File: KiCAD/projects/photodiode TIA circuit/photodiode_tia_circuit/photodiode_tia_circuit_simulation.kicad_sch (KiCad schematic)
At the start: 8 parts, among them U2 ${SIM.PARAMS}, U3 ${SIM.PARAMS}

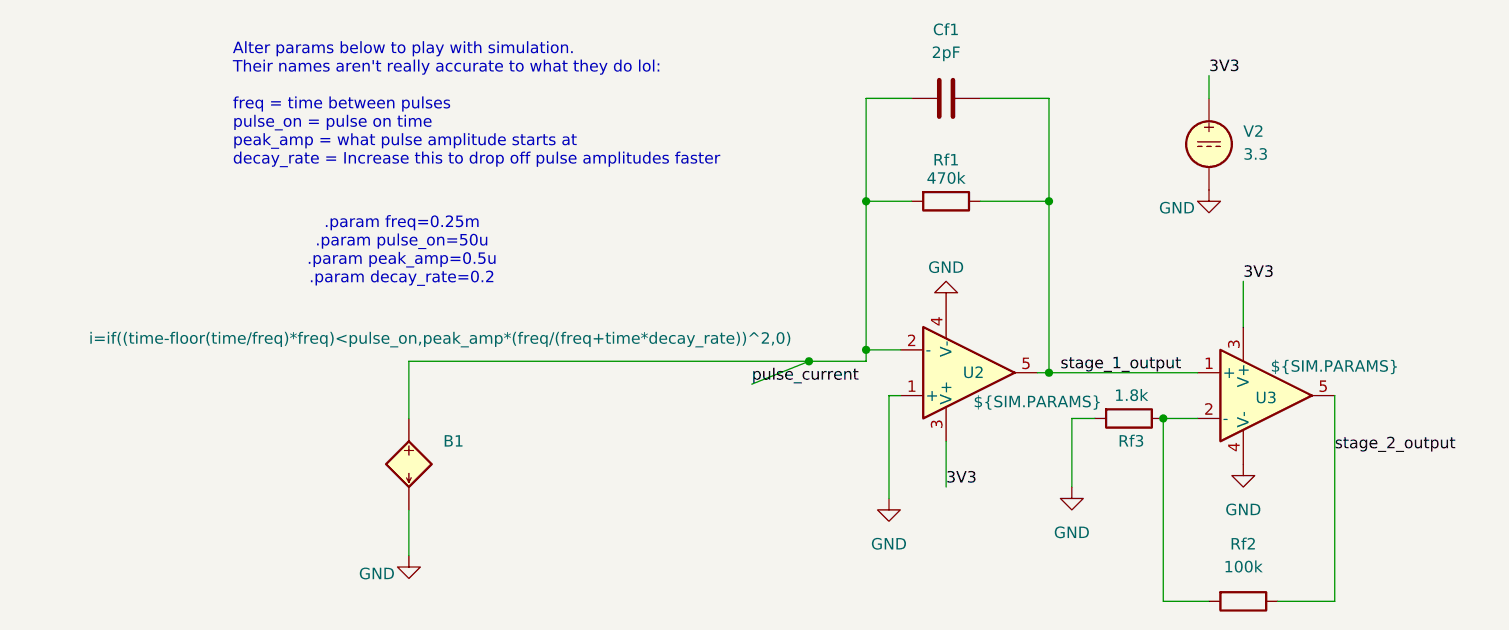
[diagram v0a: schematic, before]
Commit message: Update to make more sense and have flat-topped pulses
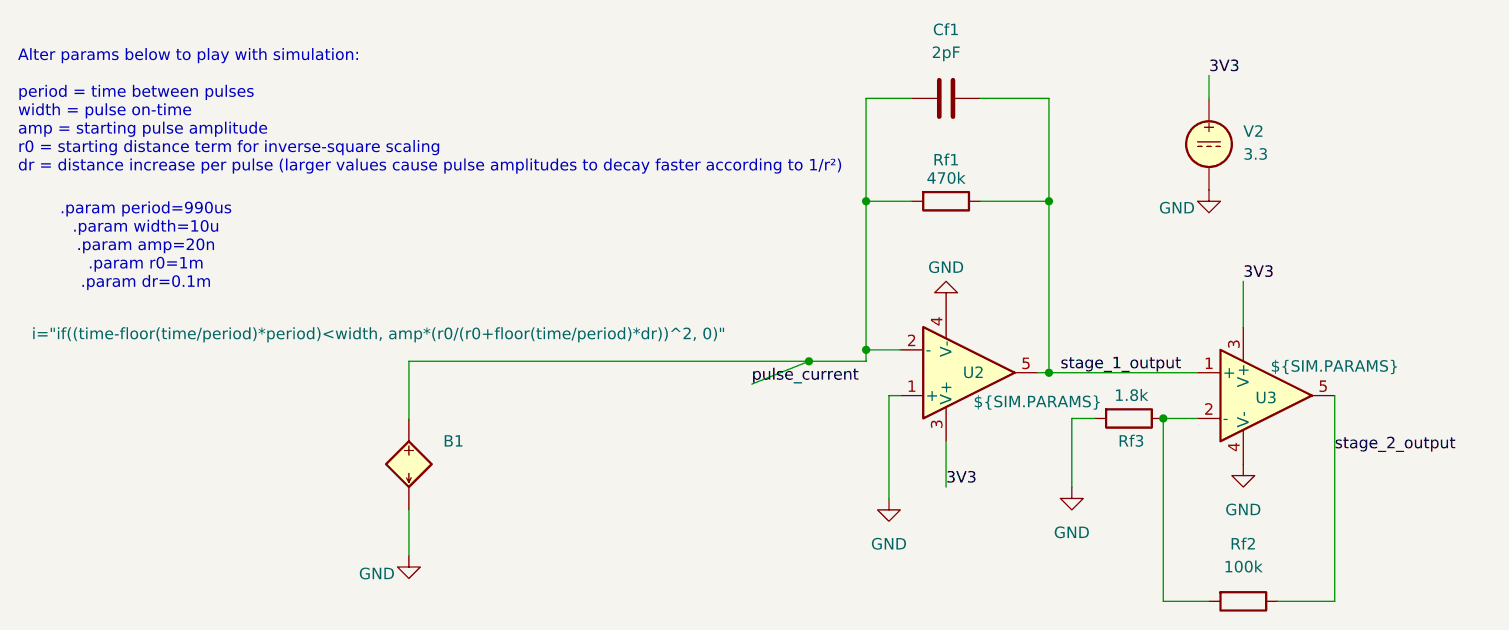
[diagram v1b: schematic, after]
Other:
- note added: ".param period=990us .param width=10u .param amp=20n .param r0=1m .param dr=0.1m"
- note added: "Alter params below to play with simulation: period = time between pulses width = pulse on-time amp = starting pulse amplitude r0 = starting distance term for inverse-square scaling dr = distance increase per pulse (larger values cause pulse amplitudes to decay faster according to 1/r²)"
- note removed: ".param freq=0.25m .param pulse_on=50u .param peak_amp=0.5u .param decay_rate=0.2"
- note removed: "Alter params below to play with simulation. Their names aren't really accurate to what they do lol: freq = time between pulses pulse_on = pulse on time peak_amp = what pulse amplitude starts at decay_rate = Increase this to drop off pulse amplitudes faster"
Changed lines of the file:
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@@
 	(generator_version "10.0")
 	(paper "A4")
-	(text ".param freq=0.25m\n.param pulse_on=50u\n.param peak_amp=0.5u\n.param decay_rate=0.2"
+	(text ".param period=990us \n.param width=10u\n.param amp=20n \n.param r0=1m \n.param dr=0.1m"
 		(exclude_from_sim no)
-		(at 62.738 103.378 0)
+		(at 34.29 102.87 0)
 		(effects
 			(font
@@
 		)
 	)
-	(text "Alter params below to play with simulation.\nTheir names aren't really accurate to what they do lol:\n\nfreq = time between pulses\npulse_on = pulse on time\npeak_amp = what pulse amplitude starts at\ndecay_rate = Increase this to drop off pulse amplitudes faster\n"
+	(text "Alter params below to play with simulation:\n\nperiod = time between pulses\nwidth = pulse on-time\namp = starting pulse amplitude\nr0 = starting distance term for inverse-square scaling\ndr = distance increase per pulse (larger values cause pulse amplitudes to decay faster according to 1/r²)"
 		(exclude_from_sim no)
-		(at 43.942 87.122 0)
+		(at 20.066 87.884 0)
 		(effects
 			(font
@@
 		)
 		(property "Value" "${SIM.PARAMS}"
-			(at 27.94 113.03 0)
+			(at 21.59 112.522 0)
 			(show_name no)
 			(do_not_autoplace no)
@@
 			)
 		)
-		(property "Sim.Params" "i=if((time-floor(time/freq)*freq)<pulse_on,peak_amp*(freq/(freq+time*decay_rate))^2,0)"
+		(property "Sim.Params" "i=\"if((time-floor(time/period)*period)<width, amp*(r0/(r0+floor(time/period)*dr))^2, 0)\""
 			(at 63.5 127 0)
 			(hide yes)

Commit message: Better yet sim
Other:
- note added: ".param period=100us .param width=10u .param amp=1m .param r0=0.1m .param dr=0.5m"
- note removed: ".param period=990us .param width=10u .param amp=20n .param r0=1m .param dr=0.1m"
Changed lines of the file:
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@@
 	(generator_version "10.0")
 	(paper "A4")
-	(text ".param period=990us \n.param width=10u\n.param amp=20n \n.param r0=1m \n.param dr=0.1m"
+	(text ".param period=100us \n.param width=10u\n.param amp=1m \n.param r0=0.1m \n.param dr=0.5m"
 		(exclude_from_sim no)
 		(at 34.29 102.87 0)

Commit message: even better sims
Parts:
- added Cf2: 2pF, Capacitor_THT:C_Disc_D10.5mm_W5.0mm_P5.00mm, symbol Device:C
- added Rf4: 100, Resistor_THT:R_Axial_DIN0207_L6.3mm_D2.5mm_P10.16mm_Horizontal, symbol Device:R
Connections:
- net GND: now also Cf2.1, Rf4.2
- net pulse_current: now also Cf2.2, Rf4.1
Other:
- note added: ".param period=100us .param width=10u .param amp=200n .param r0=1m .param dr=0.05m"
- note removed: ".param period=100us .param width=10u .param amp=1m .param r0=0.1m .param dr=0.5m"

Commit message: update
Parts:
- removed Rf4: 100, Resistor_THT:R_Axial_DIN0207_L6.3mm_D2.5mm_P10.16mm_Horizontal, symbol Device:R
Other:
- note added: ".param period=990us .param width=10u .param amp=200n .param r0=1m .param dr=0.1m"
- note removed: ".param period=100us .param width=10u .param amp=200n .param r0=1m .param dr=0.05m"
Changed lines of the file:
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@@
 	(generator_version "10.0")
 	(paper "A4")
-	(text ".param period=100us \n.param width=10u\n.param amp=200n \n.param r0=1m \n.param dr=0.05m"
+	(text ".param period=990us \n.param width=10u\n.param amp=200n \n.param r0=1m \n.param dr=0.1m"
 		(exclude_from_sim no)
 		(at 34.29 102.87 0)
@@
 	)
 	(junction
-		(at 107.95 115.57)
-		(diameter 0)
-		(color 0 0 0 0)
-	)
-	(junction
-		(at 83.82 115.57)
-		(diameter 0)
-		(color 0 0 0 0)
-	)
-	(junction
 		(at 63.5 133.35)
 		(diameter 0)
@@
 	(wire
 		(pts
-			(xy 107.95 115.57) (xy 114.3 115.57)
-		)
-		(stroke
-			(width 0)
-			(type default)
-		)
-	)
-	(wire
-		(pts
 			(xy 53.34 121.92) (xy 53.34 115.57)
 		)
@@
 	(wire
 		(pts
-			(xy 63.5 115.57) (xy 83.82 115.57)
-		)
-		(stroke
-			(width 0)
-			(type default)
-		)
-	)
-	(wire
-		(pts
 			(xy 53.34 115.57) (xy 63.5 115.57)
 		)
@@
 	(wire
 		(pts
-			(xy 83.82 115.57) (xy 107.95 115.57)
+			(xy 63.5 115.57) (xy 114.3 115.57)
 		)
 		(stroke
@@
 		(pts
 			(xy 63.5 115.57) (xy 63.5 121.92)
-		)
-		(stroke
-			(width 0)
-			(type default)
-		)
-	)
-	(wire
-		(pts
-			(xy 101.6 118.11) (xy 107.95 115.57)
 		)
 		(stroke
@@
 	)
 	(label "pulse_current"
-		(at 101.6 118.11 0)
+		(at 99.06 115.57 0)
 		(effects
 			(font
@@
 		)
 		(property "Value" "${SIM.PARAMS}"
-			(at 21.59 112.522 0)
+			(at 21.082 110.49 0)
 			(show_name no)
 			(do_not_autoplace no)
@@
 				(path "/c9490f31-99a0-4a89-8aa1-95c2524c298c"
 					(reference "#PWR015")
-					(unit 1)
-				)
-			)
-		)
-	)
-	(symbol
-		(lib_id "power:GND")
-		(at 83.82 123.19 0)
-		(unit 1)
-		(body_style 1)
-		(exclude_from_sim no)
-		(in_bom yes)
-		(on_board yes)
-		(in_pos_files yes)
-		(dnp no)
-		(fields_autoplaced yes)
-		(property "Reference" "#PWR016"
-			(at 83.82 129.54 0)
-			(hide yes)
-			(show_name no)
-			(do_not_autoplace no)
-			(effects
-				(font
-					(size 1.27 1.27)
-				)
-			)
-		)
-		(property "Value" "GND"
-			(at 83.82 128.27 0)
-			(show_name no)
-			(do_not_autoplace no)
-			(effects
-				(font
-					(size 1.27 1.27)
-				)
-			)
-		)
-		(property "Footprint" ""
-			(at 83.82 123.19 0)
-			(hide yes)
-			(show_name no)
-			(do_not_autoplace no)
-			(effects
-				(font
-					(size 1.27 1.27)
-				)
-			)
-		)
-		(property "Datasheet" ""
-			(at 83.82 123.19 0)
-			(hide yes)
-			(show_name no)
-			(do_not_autoplace no)
-			(effects
-				(font
-					(size 1.27 1.27)
-				)
-			)
-		)
-		(property "Description" "Power symbol creates a global label with name \"GND\" , ground"
-			(at 83.82 123.19 0)
-			(hide yes)
-			(show_name no)
-			(do_not_autoplace no)
-			(effects
-				(font
-					(size 1.27 1.27)
-				)
-			)
-		)
-		(pin "1"
-		)
-		(instances
-			(project "photodiode_tia_circuit_simulation"
-				(path "/c9490f31-99a0-4a89-8aa1-95c2524c298c"
-					(reference "#PWR016")
 					(unit 1)
 				)
@@
 					(unit 1)
 				)
-			)
-		)
-	)
-	(symbol
-		(lib_id "Device:R")
-		(at 83.82 119.38 0)
-		(unit 1)
-		(body_style 1)
-		(exclude_from_sim no)
-		(in_bom yes)
-		(on_board yes)
-		(in_pos_files yes)
-		(dnp no)
-		(property "Reference" "Rf4"
-			(at 89.408 119.126 0)
-			(show_name no)
-			(do_not_autoplace no)
-			(effects
-				(font
-					(size 1.27 1.27)
-				)
-			)
-		)
-		(property "Value" "100"
-			(at 90.17 122.174 0)
-			(show_name no)
-			(do_not_autoplace no)
-			(effects
-				(font
-					(size 1.27 1.27)
-				)
-			)
-		)
-		(property "Footprint" "Resistor_THT:R_Axial_DIN0207_L6.3mm_D2.5mm_P10.16mm_Horizontal"
-			(at 82.042 119.38 90)
-			(hide yes)
-			(show_name no)
-			(do_not_autoplace no)
-			(effects
-				(font
-					(size 1.27 1.27)
-				)
-			)
-		)
-		(property "Datasheet" ""
-			(at 83.82 119.38 0)
-			(hide yes)
-			(show_name no)
-			(do_not_autoplace no)
-			(effects
-				(font
-					(size 1.27 1.27)
-				)
-			)
-		)
-		(property "Description" "Resistor"
-			(at 83.82 119.38 0)
-			(hide yes)
-			(show_name no)
-			(do_not_autoplace no)
-			(effects
-				(font
-					(size 1.27 1.27)
-				)
-			)
-		)
-		(pin "1"
-		)
-		(pin "2"
-		)
-		(instances
-			(project "photodiode_tia_circuit_simulation"
-				(path "/c9490f31-99a0-4a89-8aa1-95c2524c298c"
-					(reference "Rf4")
-					(unit 1)
-				)
